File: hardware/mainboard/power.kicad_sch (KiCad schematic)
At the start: 59 parts, among them Q4 BSS138, Q6 FDN340P, U3 AP6230xWU, U4 AP6230xWU, U5 SiC438, U6 AP6230xWU, U7 AP6230xWU

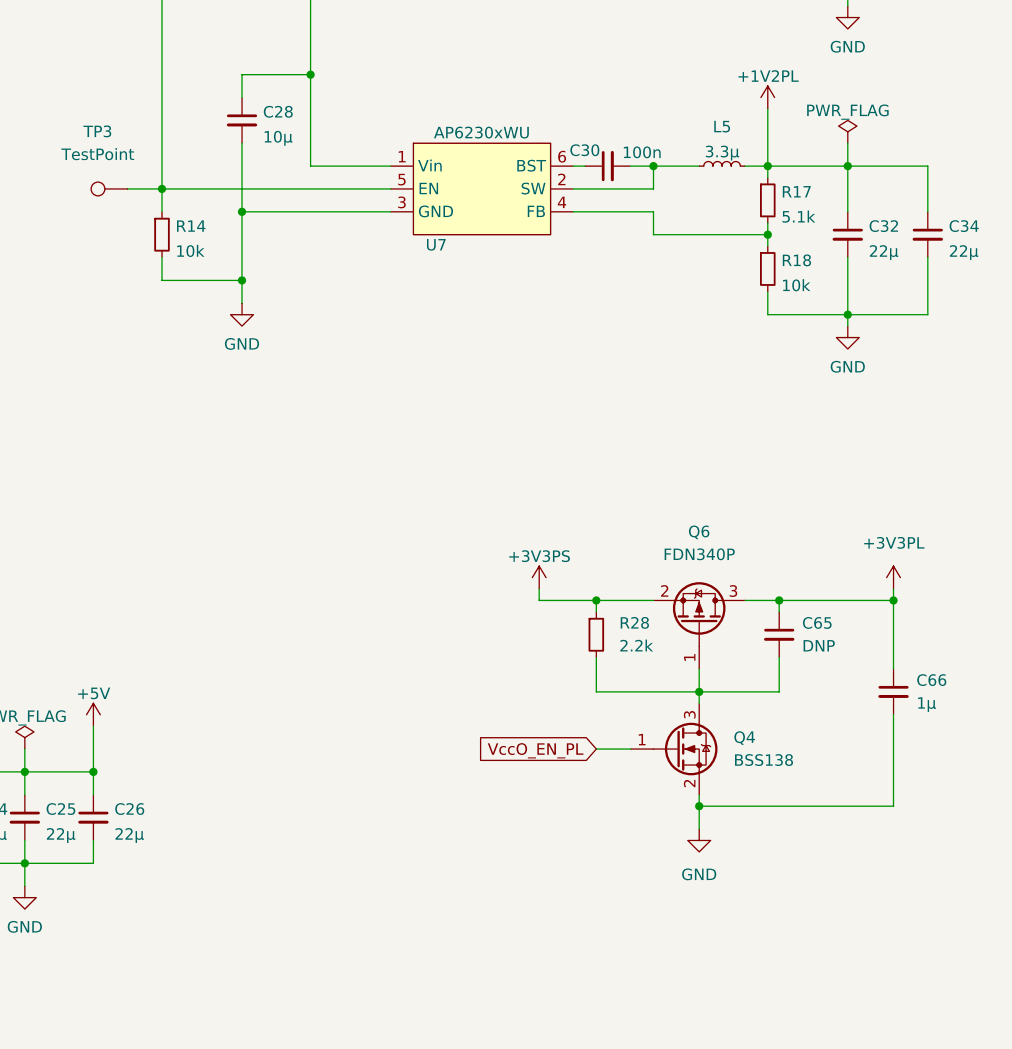
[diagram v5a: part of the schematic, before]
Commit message: Add separate reg for 3V3PL
Signed-off-by: gatecat <gatecat@ds0.me>
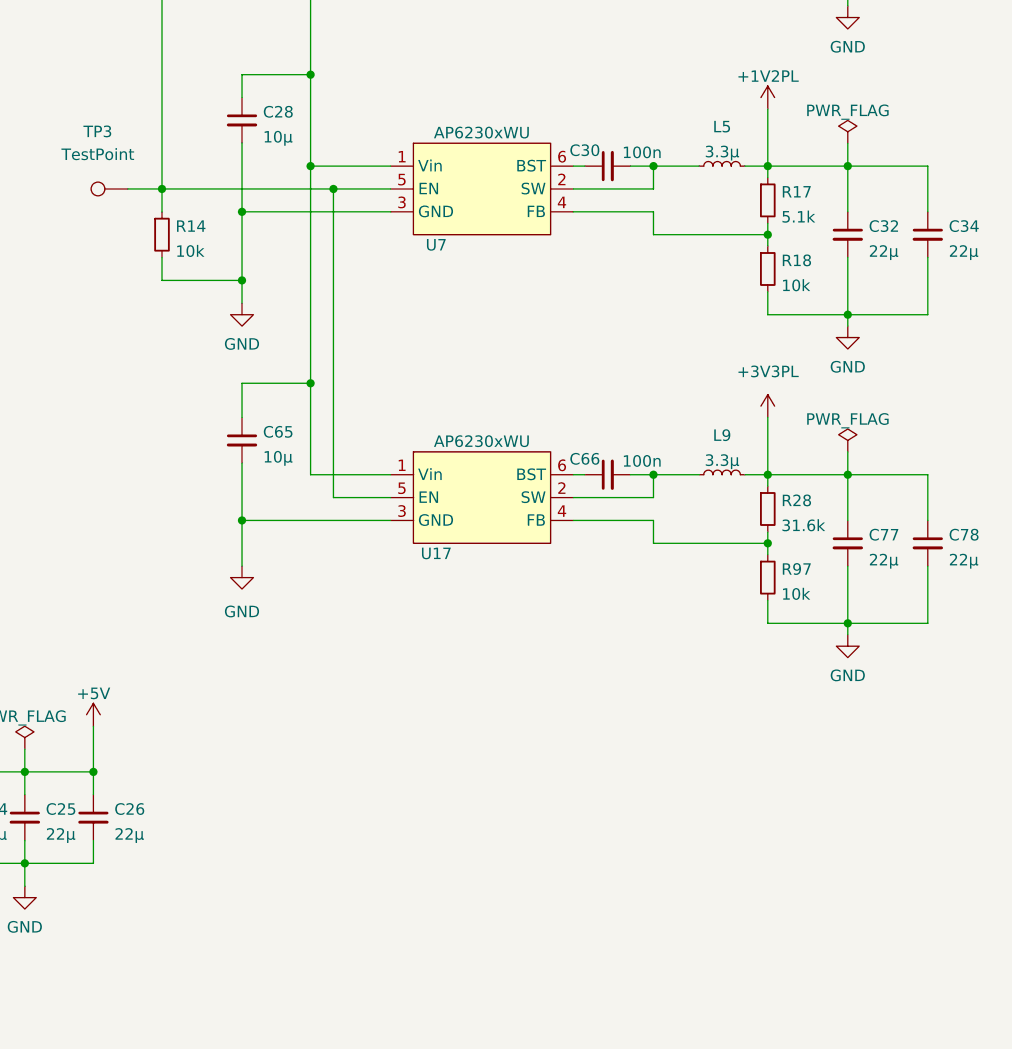
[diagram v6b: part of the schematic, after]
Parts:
- removed Q4: BSS138, Package_TO_SOT_SMD:SOT-23, symbol Transistor_FET:BSS138
- removed Q6: FDN340P, Package_TO_SOT_SMD:SOT-23, symbol Transistor_FET:FDN340P
- added C77, C78: 22µ, Capacitor_SMD:C_1206_3216Metric, symbol Device:C_Small
- added L9: 3.3µ, meowality:BWVS00606045, symbol Device:L_Small
- added R97: 10k, Resistor_SMD:R_0402_1005Metric, symbol Device:R_Small
- added U17: AP6230xWU, Package_TO_SOT_SMD:TSOT-23-6, symbol meowality:AP6230xWU
- C65: value DNP -> 10µ; footprint Capacitor_SMD:C_0603_1608Metric -> Capacitor_SMD:C_1206_3216Metric
- C66: value 1µ -> 100n; footprint Capacitor_SMD:C_0603_1608Metric -> Capacitor_SMD:C_0402_1005Metric
- R28: value 2.2k -> 31.6k
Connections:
- net +3V3PS: no longer C65.1, C66.1, R28.1
- net +5V: now also C65.1, U17.1 (Vin)
- net GND: now also C65.2, C77.2, C78.2, R97.2, U17.3 (GND); no longer C66.2
- net VccO_EN_PL: now also U17.5 (EN)
- net at R28.2: now also R97.1, U17.4 (FB); no longer C65.2
- new net: C66.1, U17.6 (BST)
- new net: C66.2, L9.1, U17.2 (SW)
- new net +3V3PL: C77.1, C78.1, L9.2, R28.1

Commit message: Placement snapshot
Signed-off-by: gatecat <gatecat@ds0.me>
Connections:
- net SiC_V_{DD}: now also U5.15 (V_{DD}); no longer U5.12 (V_{DRV})
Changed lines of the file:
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@@
     (pin "11")
-    (pin "12")
     (pin "12")
     (pin "13")
     (pin "14")
+    (pin "15")
     (pin "16")
     (pin "17")

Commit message: Placement snapshot 3
Signed-off-by: gatecat <gatecat@ds0.me>
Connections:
- net SiC_V_{DD}: now also U5.12 (V_{DRV}); no longer U5.15 (V_{DD})
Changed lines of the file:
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@@
     (pin "11")
+    (pin "12")
     (pin "12")
     (pin "13")
     (pin "14")
-    (pin "15")
     (pin "16")
     (pin "17")
